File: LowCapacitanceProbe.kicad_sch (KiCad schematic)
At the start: 39 parts, among them J1 u.Fl, J2 SMA, Q1 BF998, U1 SPX3819M5-L

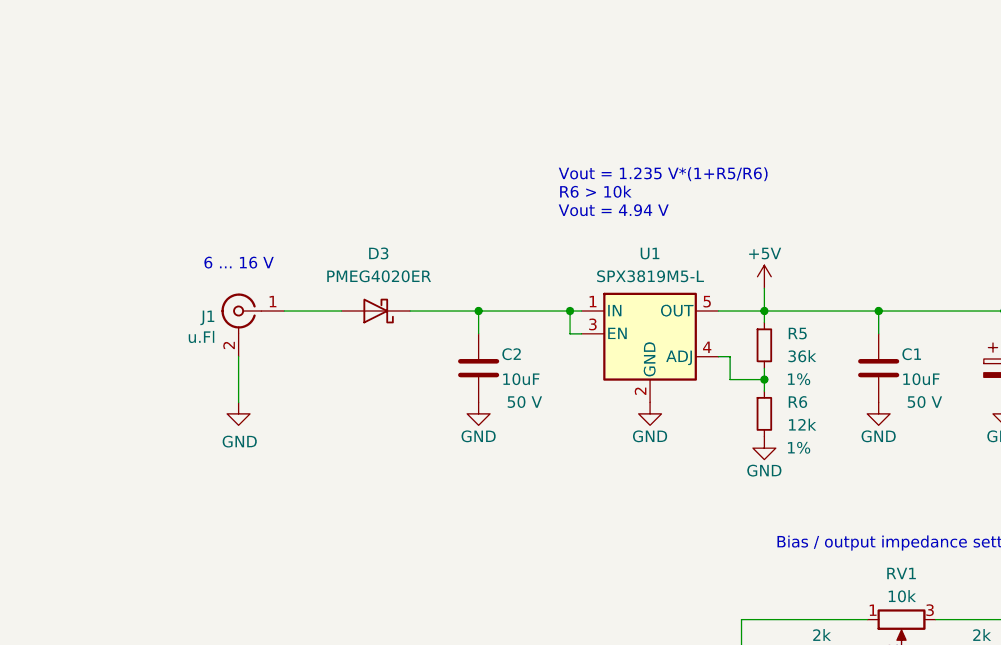
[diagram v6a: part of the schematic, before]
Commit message: Reduced peak current during connection of power, replaced LDO from adjustable version by 5V, lowered noise of LDO.
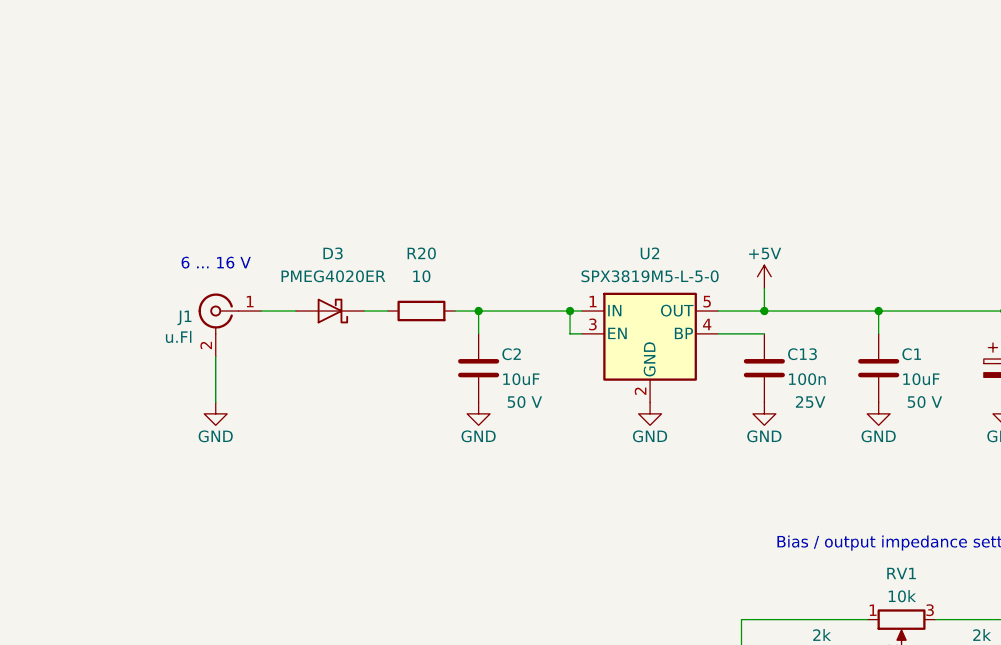
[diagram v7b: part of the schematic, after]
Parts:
- removed R5: 36k, Resistor_SMD:R_0603_1608Metric_Pad0.98x0.95mm_HandSolder, symbol Device:R_Small
- removed R6: 12k, Resistor_SMD:R_0603_1608Metric_Pad0.98x0.95mm_HandSolder, symbol Device:R_Small
- removed U1: SPX3819M5-L, Package_TO_SOT_SMD:SOT-23-5, symbol Regulator_Linear:SPX3819M5-L
- added C13: 100n, Capacitor_SMD:C_0603_1608Metric_Pad1.08x0.95mm_HandSolder, symbol Device:C
- added R20: 10, Resistor_SMD:R_1206_3216Metric_Pad1.30x1.75mm_HandSolder, symbol Device:R
- added U2: SPX3819M5-L-5-0, Package_TO_SOT_SMD:SOT-23-5, symbol Regulator_Linear:SPX3819M5-L-5-0
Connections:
- net +5V: now also U2.5 (OUT)
- net GND: now also C13.1, U2.2 (GND)
- net at C2.2: now also R20.2, U2.1 (IN), U2.3 (EN); no longer D3.1 (K)
- new net: D3.1 (K), R20.1
- new net: C13.2, U2.4 (BP)
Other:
- note removed: "Vout = 1.235 V*(1+R5/R6) R6 > 10k Vout = 4.94 V"
- moved on the sheet: D3, J1

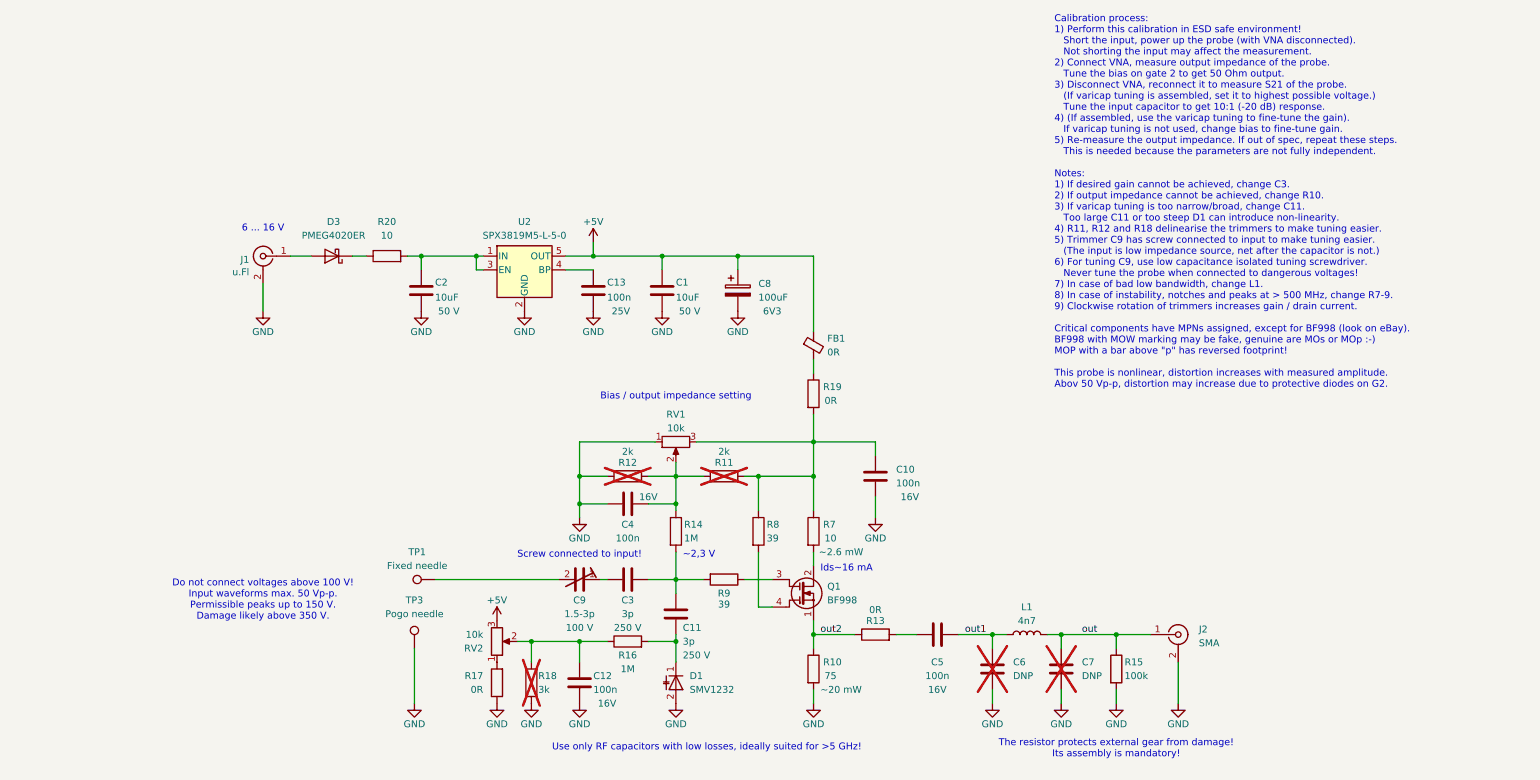
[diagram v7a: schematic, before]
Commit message: Added net labels, synchronised PCB with SCH, grouped all elements.
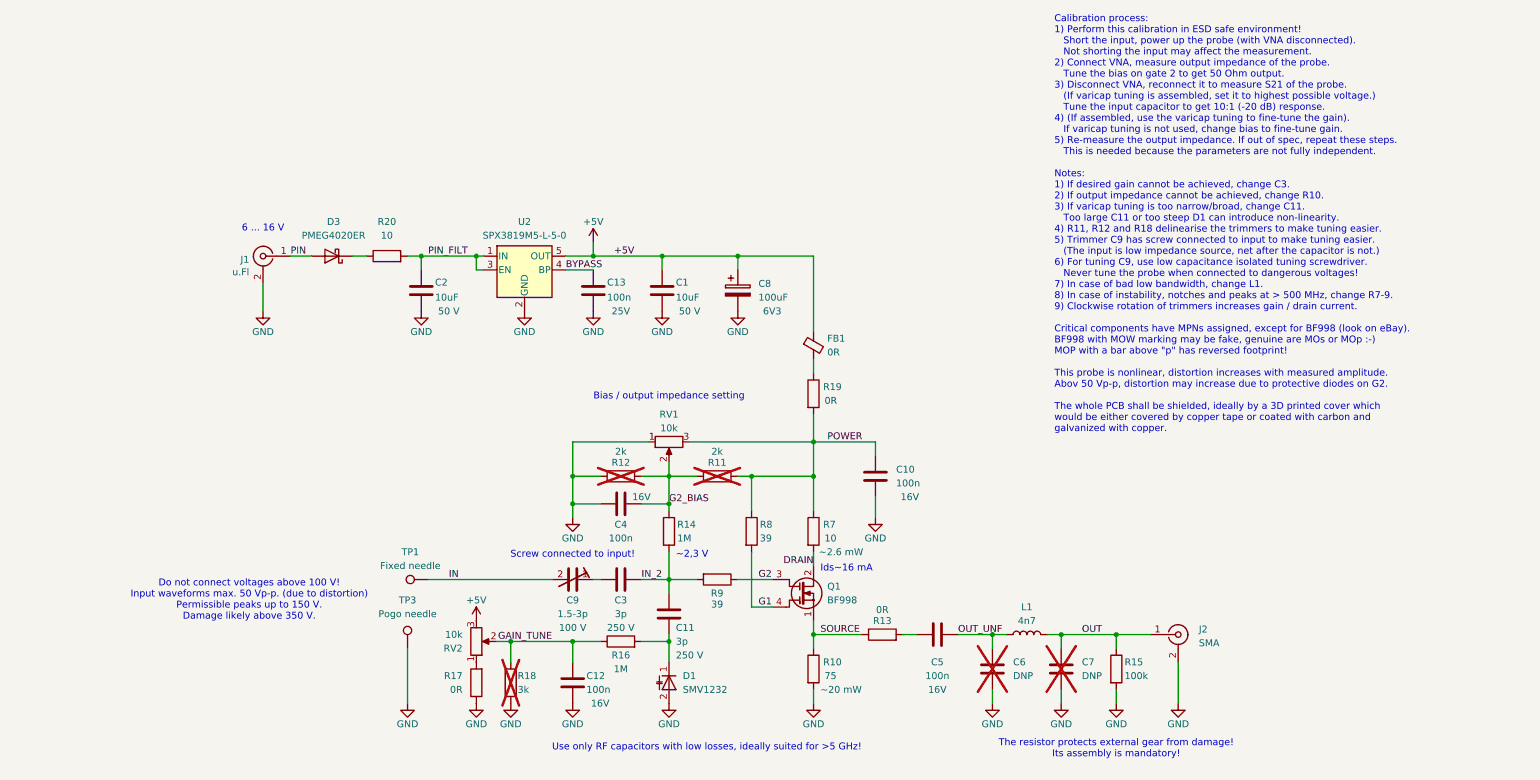
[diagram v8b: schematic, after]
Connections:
- net PIN_FILT: now reaches C2.2, R20.2, U2.1 (IN), U2.3 (EN)
- net IN_2: now reaches C11.2, C3.2, R14.2, R9.2
- net GAIN_TUNE: now reaches C12.2, R16.1, R18.2, RV2.2
- net POWER: now reaches C10.2, R11.2, R19.2, R7.1, R8.1, RV1.3
- net G2_BIAS: now reaches C4.1, R11.1, R12.2, R14.1, RV1.2
- net DRAIN: now reaches Q1.2 (D), R7.2
- net G2: now reaches Q1.3 (G1), R9.1
- net G1: now reaches Q1.4 (G2), R8.2
- net PIN: now reaches D3.2 (A), J1.1 (In)
- net IN: now reaches C9.2, TP1.1
- net BYPASS: now reaches C13.2, U2.4 (BP)
- net out renamed OUT
- net out1 renamed OUT_UNF
- net out2 renamed SOURCE
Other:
- note added: "Do not connect voltages above 100 V! Input waveforms max. 50 Vp-p. (due to distortion) Permissible peaks up to 150 V. Damage likely above 350 V."
- note removed: "Do not connect voltages above 100 V! Input waveforms max. 50 Vp-p. Permissible peaks up to 150 V. Damage likely above 350 V."
- moved on the sheet: C11, C12, C3, C4, C9, D1, R11, R12, R13, R14, R16, R17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
